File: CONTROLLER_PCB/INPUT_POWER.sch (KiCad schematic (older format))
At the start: 61 parts

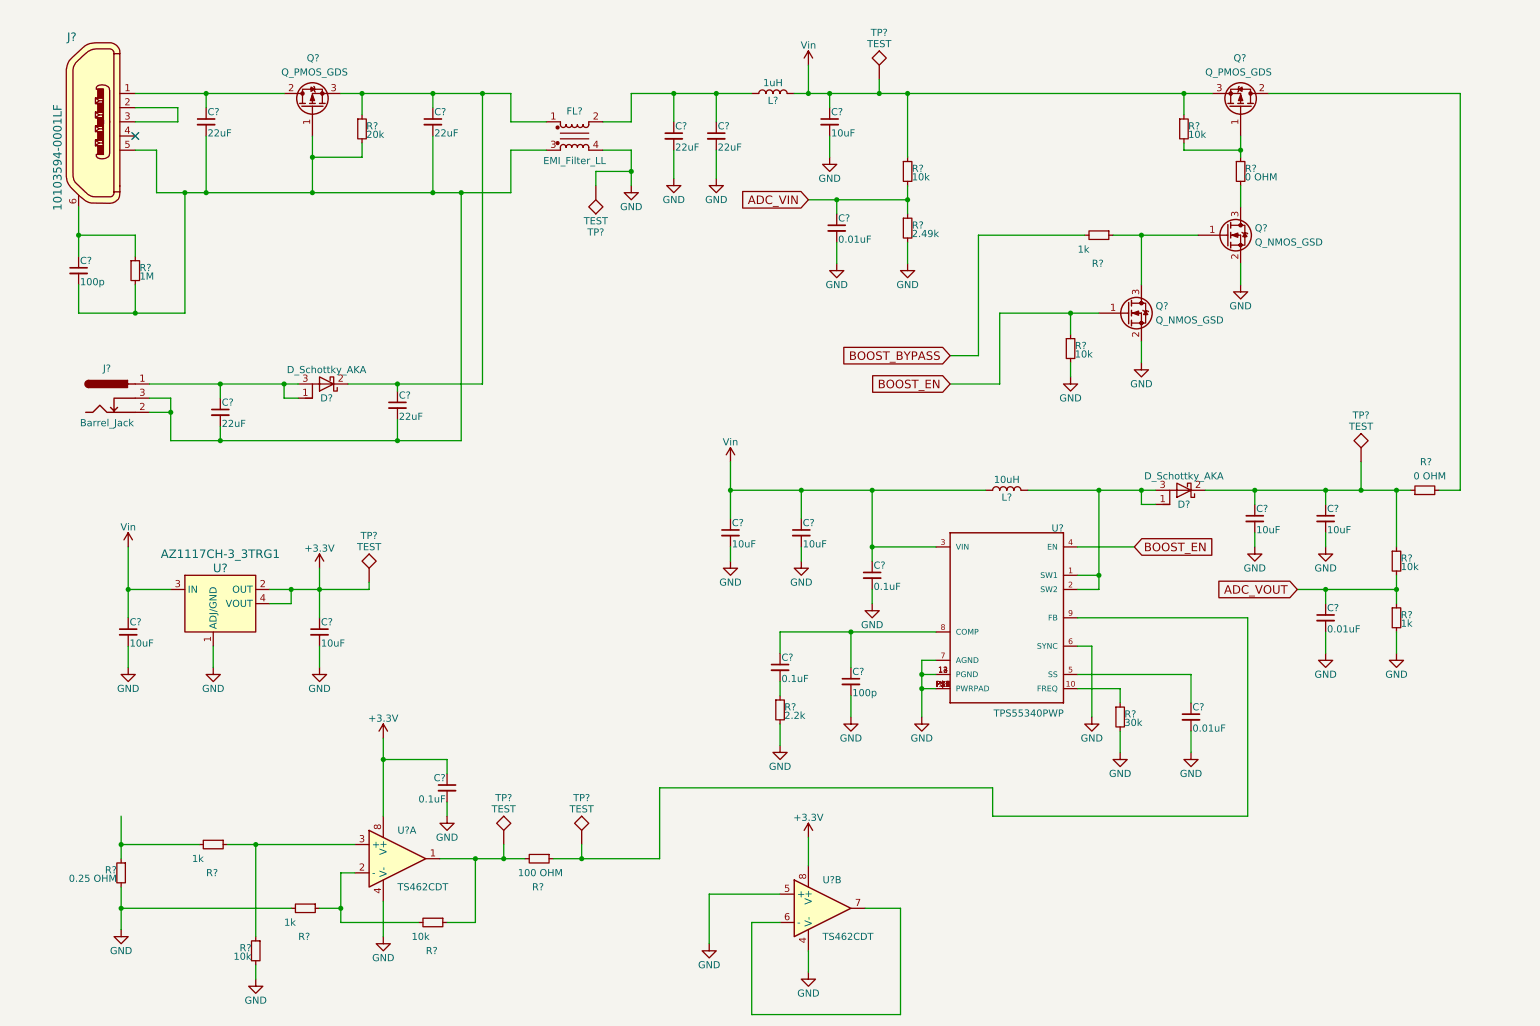
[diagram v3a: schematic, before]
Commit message: Finalized schematic, created BOM, started placement (no PCB size yet)
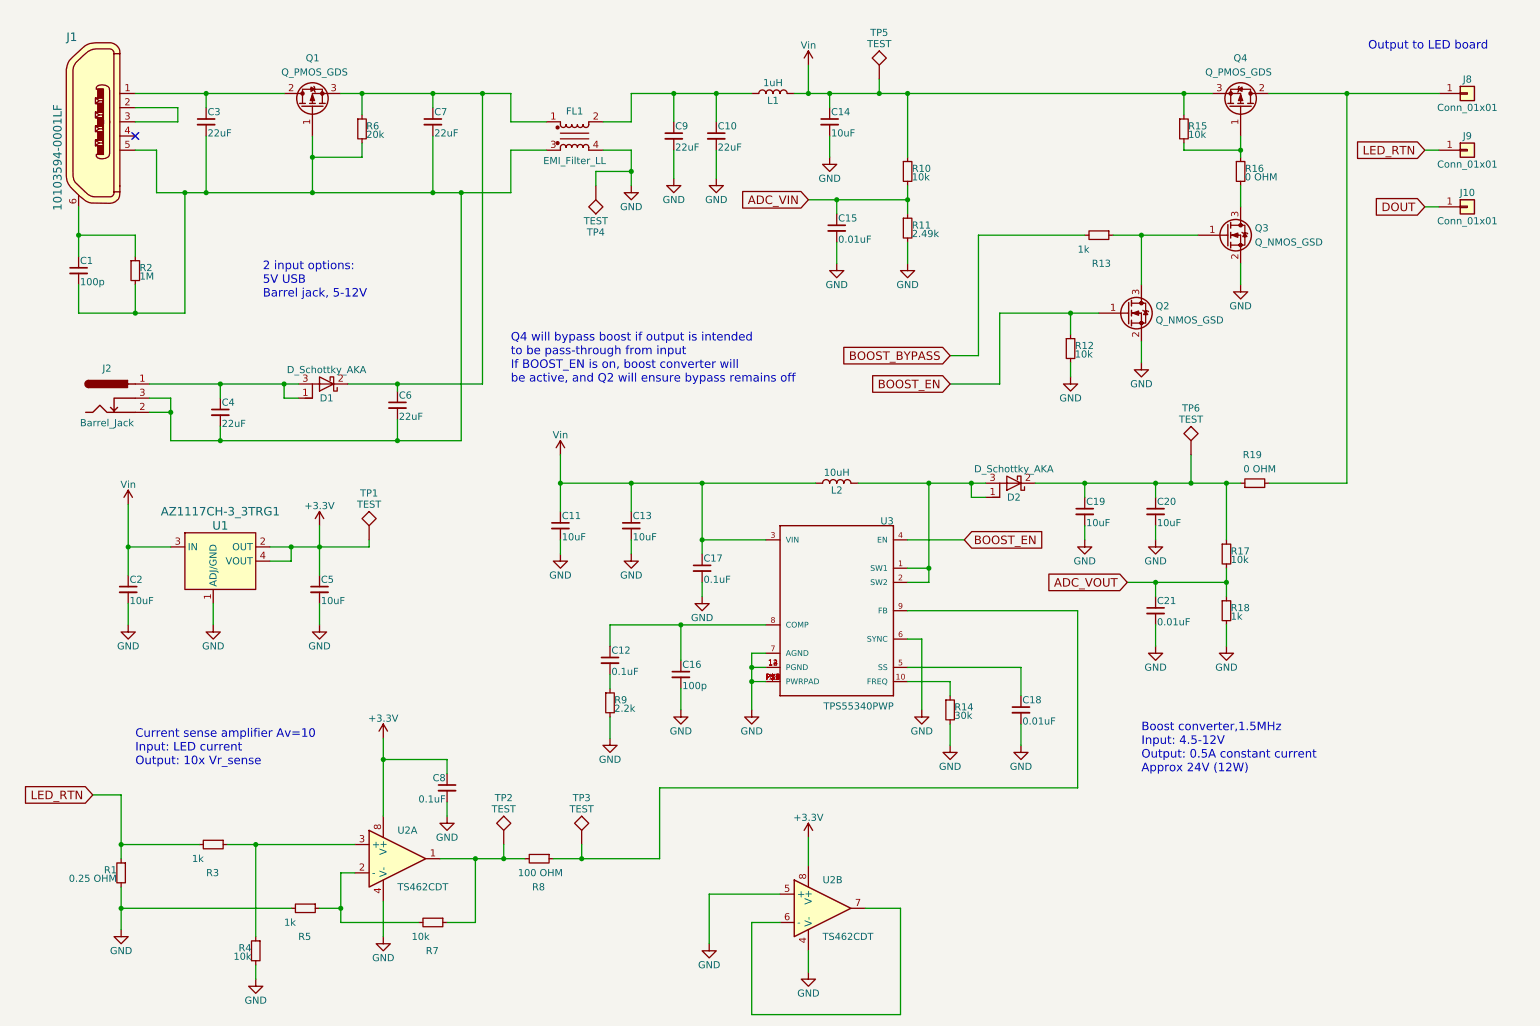
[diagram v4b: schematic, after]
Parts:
- added J10, J8, J9: Conn_01x01, Connectors:1pin, symbol Conn_01x01
- TP1: renamed from TP?; footprint (none) -> Measurement_Points:Measurement_Point_Round-SMD-Pad_Small
- U3: renamed from U?; footprint SOP65P640X120-15N -> CustomFootprints:SOP65P640X120-15N_HAND_SOLDERING
- gave numbers to parts that had none: 58
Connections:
- net LED_RTN: now reaches R1.1, R3.2
- net LED_RTN: now also J9.1 (Pin_1)
- net at Q4.2 (D), R19.2: now also J8.1 (Pin_1)
- new net DOUT: J10.1 (Pin_1)
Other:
- note added: "2 input options:\n5V USB\nBarrel jack, 5-12V"
- note added: "Boost converter,1.5MHz\nInput: 4.5-12V\nOutput: 0.5A constant current\nApprox 24V (12W)"
- note added: "Current sense amplifier Av=10\nInput: LED current\nOutput: 10x Vr_sense"
- note added: "Output to LED board"
- note added: "Q4 will bypass boost if output is intended \nto be pass-through from input\nIf BOOST_EN is on, boost converter will \nbe active, and Q2 will ensure bypass remains off"
- moved on the sheet: C11, C12, C13, C16, C17, C18, C19, C2, C20, C21, C5, D2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

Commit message: Split up power supply and MCU into 2 different boards, schematic design not complete.
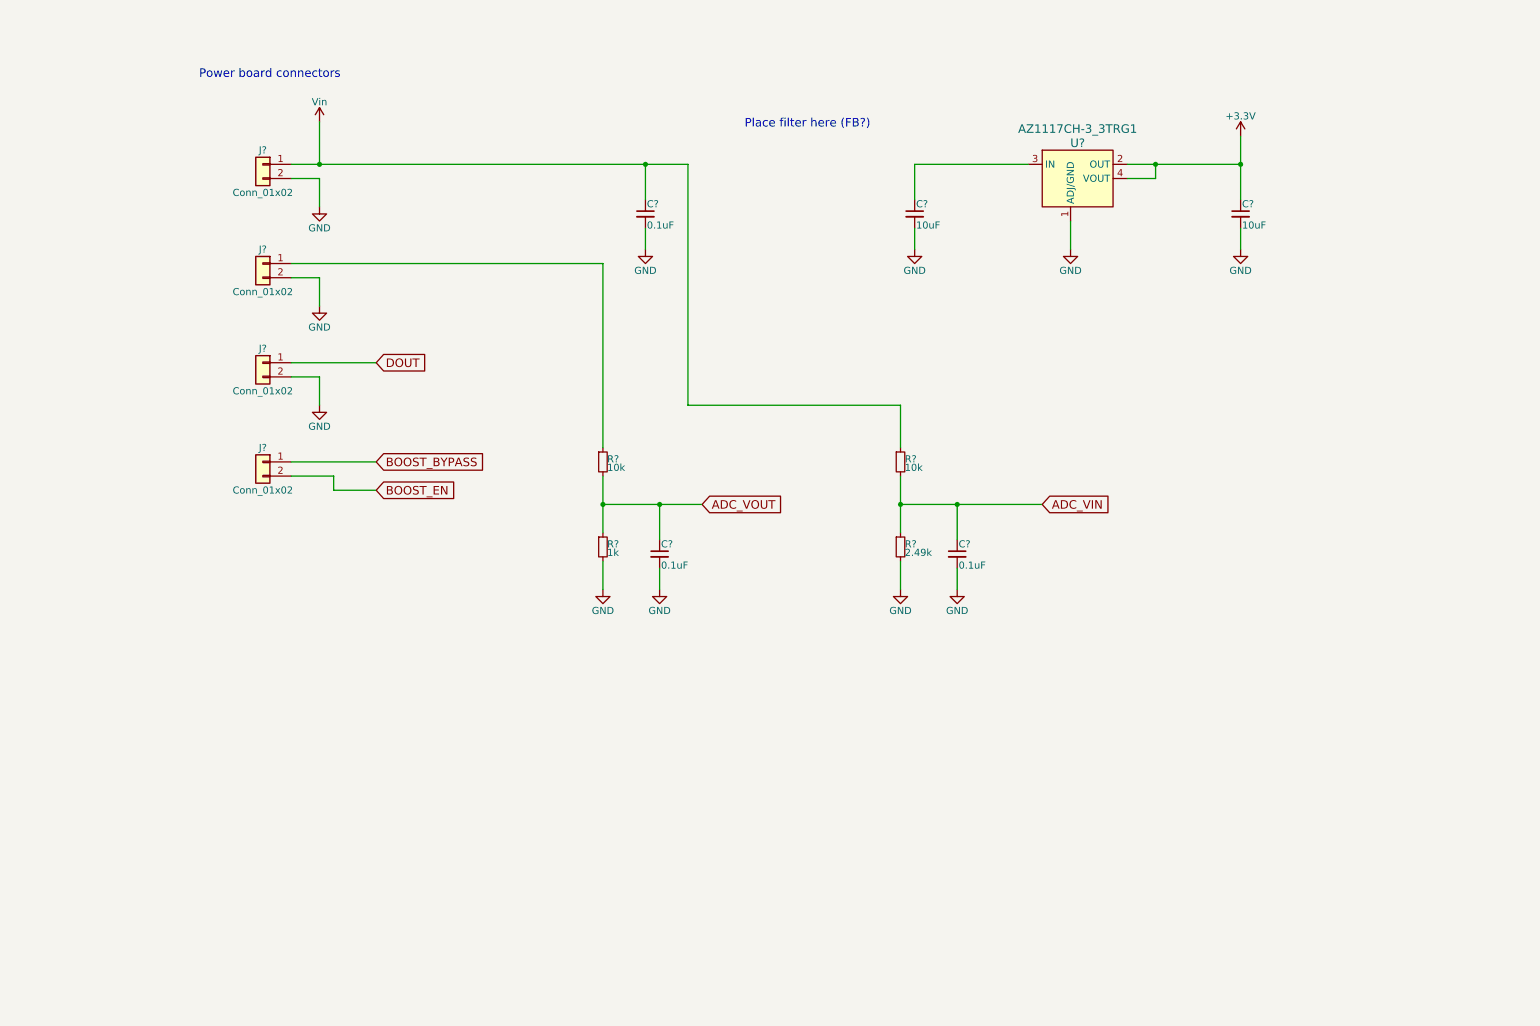
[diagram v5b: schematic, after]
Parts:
- removed C1, C16: 100p, Capacitors_SMD:C_0603_HandSoldering, symbol C_Small
- removed C10, C3, C4, C6, C7, C9: 22uF, Capacitors_SMD:C_1206_HandSoldering, symbol C_Small
- removed C11, C13, C14, C19, C2, C20, C5: 10uF, Capacitors_SMD:C_0805_HandSoldering, symbol C_Small
- removed C12, C17, C8: 0.1uF, Capacitors_SMD:C_0603_HandSoldering, symbol C_Small
- removed C15, C18, C21: 0.01uF, Capacitors_SMD:C_0603_HandSoldering, symbol C_Small
- removed D1, D2: D_Schottky_AKA, PowerDI5:Diodes_Incorporated_POWERDI_5, symbol D_Schottky_AKA
- removed FL1: EMI_Filter_LL, CustomFootprints:IND_ACM12V-701-2PL-TL00_FixedPadNumbers, symbol EMI_Filter_LL
- removed J1: 10103594-0001LF, Connectors:USB_Micro-B_10103594-0001LF, symbol 10103594-0001LF
- removed J10, J8, J9: Conn_01x01, Connectors:1pin, symbol Conn_01x01
- removed J2: Barrel_Jack, Connectors:BARREL_JACK, symbol Barrel_Jack
- removed L1: 1uH, CustomFootprints:L_12x12mm_h8mm_hand_soldering, symbol L
- removed L2: 10uH, CustomFootprints:L_12x12mm_h8mm_hand_soldering, symbol L
- removed Q1, Q4: Q_PMOS_GDS, TO_SOT_Packages_SMD:TO-252-2_Rectifier, symbol Q_PMOS_GDS
- removed Q2, Q3: Q_NMOS_GSD, TO_SOT_Packages_SMD:SOT-23, symbol Q_NMOS_GSD
- removed R1: 0.25 OHM, Resistors_SMD:R_1206_HandSoldering, symbol R_Small
- removed R10, R12, R15, R17, R4, R7: 10k, Resistors_SMD:R_0603_HandSoldering, symbol R_Small
- removed R11: 2.49k, Resistors_SMD:R_0603_HandSoldering, symbol R_Small
- removed R13, R18, R3, R5: 1k, Resistors_SMD:R_0603_HandSoldering, symbol R_Small
- removed R14: 30k, Resistors_SMD:R_0603_HandSoldering, symbol R_Small
- removed R16, R19: 0 OHM, Resistors_SMD:R_0603_HandSoldering, symbol R_Small
- removed R2: 1M, Resistors_SMD:R_0603_HandSoldering, symbol R_Small
- removed R6: 20k, Resistors_SMD:R_0603_HandSoldering, symbol R_Small
- removed R8: 100 OHM, Resistors_SMD:R_0603_HandSoldering, symbol R_Small
- removed R9: 2.2k, Resistors_SMD:R_0603_HandSoldering, symbol R_Small
- removed TP1, TP2, TP3, TP4, TP5, TP6: TEST, Measurement_Points:Measurement_Point_Round-SMD-Pad_Small, symbol TEST
- removed U1: AZ1117CH-3_3TRG1, digikey-footprints:SOT-223, symbol AZ1117CH-3_3TRG1
- removed U2: TS462CDT, digikey-footprints:SOIC-8_W3.9mm, symbol TS462CDT
- removed U3: TPS55340PWP, CustomFootprints:SOP65P640X120-15N_HAND_SOLDERING, symbol TPS55340PWP
- added C? (x2): 10uF, Capacitors_SMD:C_0805_HandSoldering, symbol C_Small
- added C? (x3): 0.1uF, Capacitors_SMD:C_0603_HandSoldering, symbol C_Small
- added J? (x4): Conn_01x02, symbol Conn_01x02
- added R? (x2): 10k, Resistors_SMD:R_0603_HandSoldering, symbol R_Small
- added R?: 1k, Resistors_SMD:R_0603_HandSoldering, symbol R_Small
- added R?: 2.49k, Resistors_SMD:R_0603_HandSoldering, symbol R_Small
- added U?: AZ1117CH-3_3TRG1, digikey-footprints:SOT-223, symbol AZ1117CH-3_3TRG1
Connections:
- net +3V3: now also C?.1, U?.2 (OUT), U?.4 (VOUT)
- net ADC_VIN: now also C?.1, R?.1, R?.2
- net ADC_VOUT: now also C?.1, R?.1, R?.2
- net BOOST_BYPASS: now also J?.1 (Pin_1)
- net BOOST_EN: now also J?.2 (Pin_2)
- net DOUT: now also J?.1 (Pin_1)
- net GND: now also C?.2, C?.2, C?.2, C?.2, C?.2, J?.2 (Pin_2), J?.2 (Pin_2), J?.2 (Pin_2), R?.2, R?.2, U?.1 (ADJ/GND)
- net Vin: now also C?.1, J?.1 (Pin_1), R?.1
- new net: J?.1 (Pin_1), R?.1
- new net: C?.1, U?.3 (IN)
- no-connect marks 1 -> 0
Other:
- note added: "Place filter here (FB?)"
- note added: "Power board connectors"
- note removed: "2 input options:\n5V USB\nBarrel jack, 5-12V"
- note removed: "Boost converter,1.5MHz\nInput: 4.5-12V\nOutput: 0.5A constant current\nApprox 24V (12W)"
- note removed: "Current sense amplifier Av=10\nInput: LED current\nOutput: 10x Vr_sense"
- note removed: "Output to LED board"
- note removed: "Q4 will bypass boost if output is intended \nto be pass-through from input\nIf BOOST_EN is on, boost converter will \nbe active, and Q2 will ensure bypass remains off"
